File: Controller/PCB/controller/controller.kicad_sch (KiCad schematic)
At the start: 63 parts

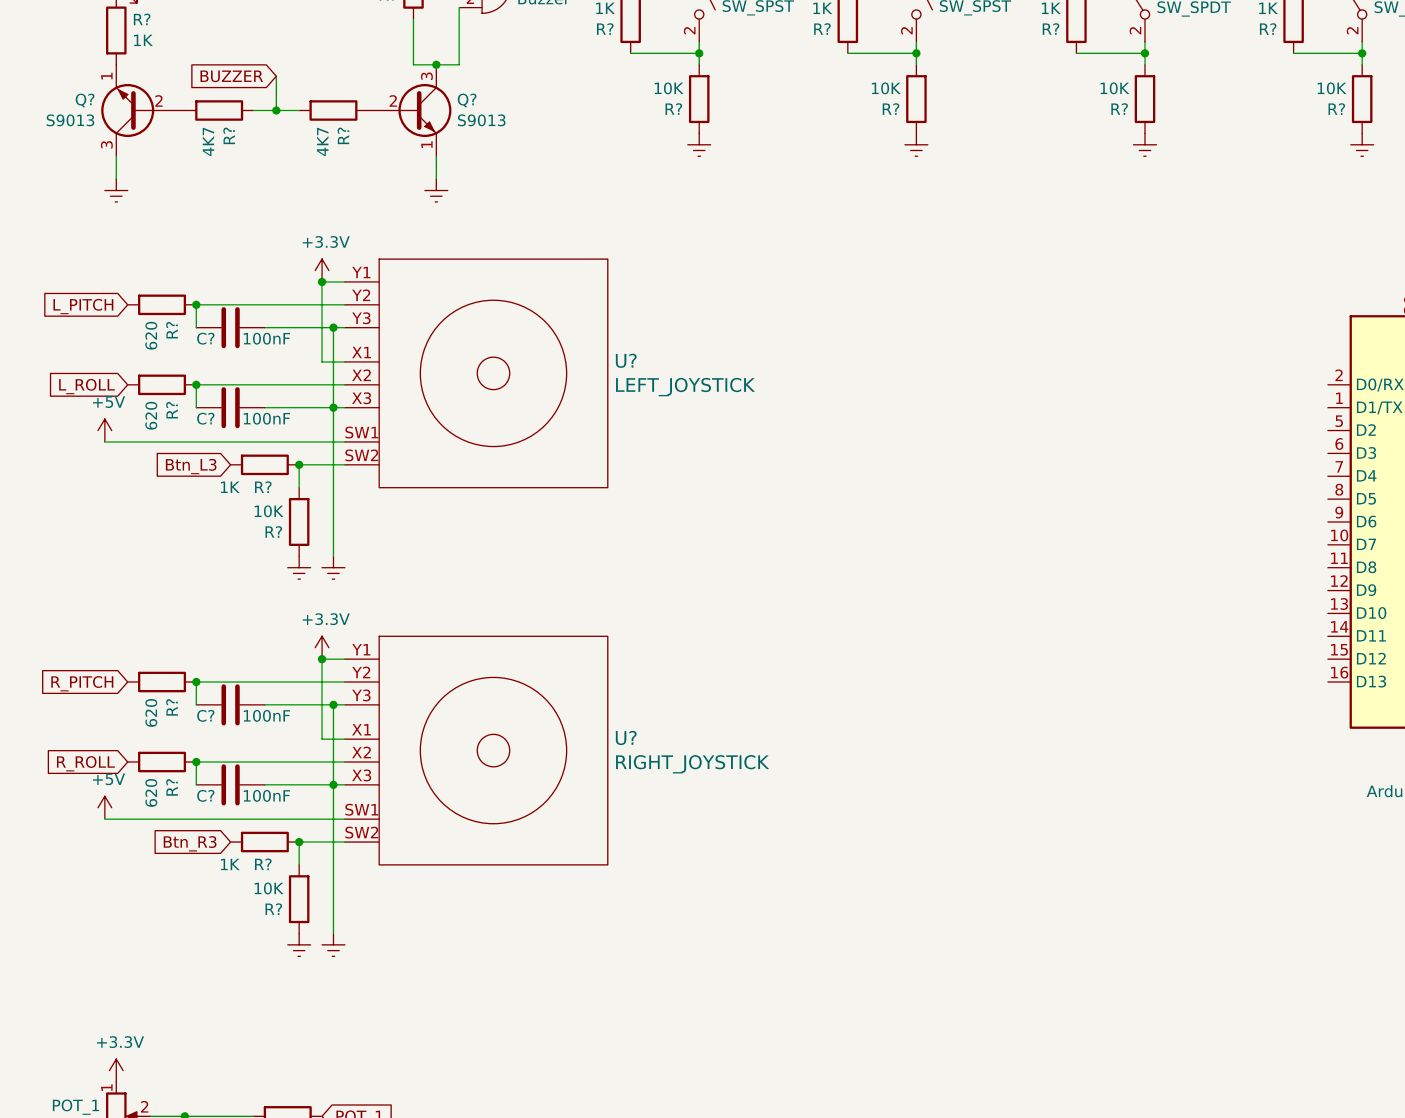
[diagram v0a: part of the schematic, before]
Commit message: Update git ignore and add make switches separate from the controller
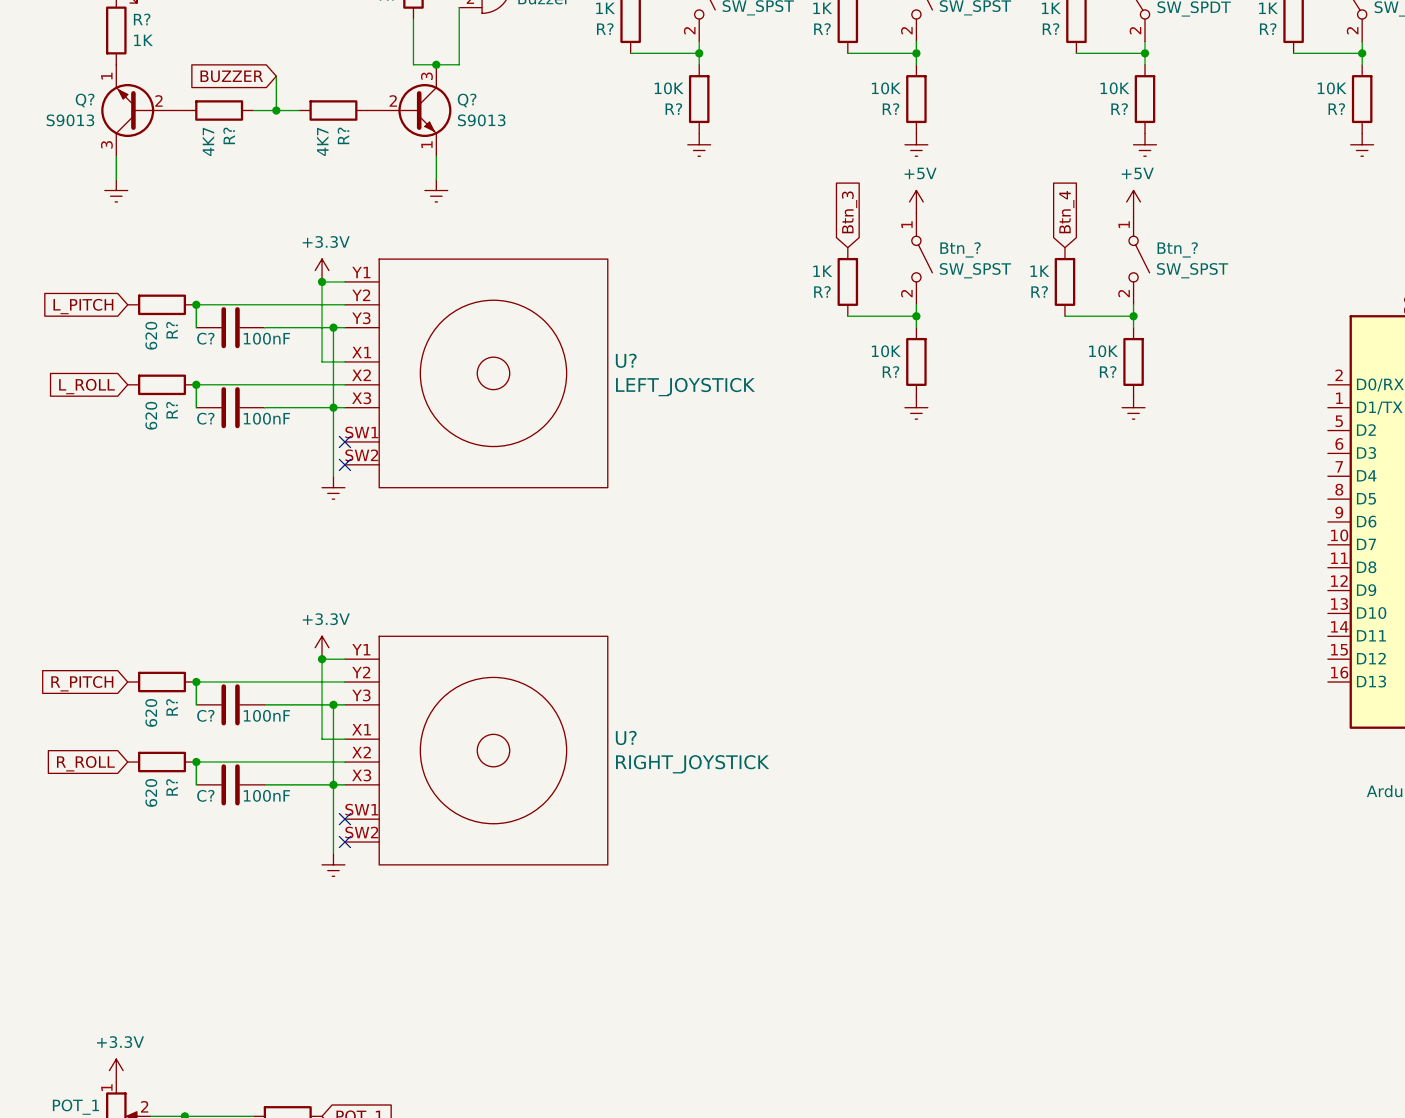
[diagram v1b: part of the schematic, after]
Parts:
- removed R? (x2): 1K, symbol Device:R
- removed R? (x2): 10K, symbol Device:R
- added Btn_? (x2): SW_SPST, symbol Switch:SW_SPST
- added R? (x2): 1K, symbol Device:R
- added R? (x2): 10K, symbol Device:R
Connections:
- net +5V: now also Btn_?.1 (A), Btn_?.1 (A); no longer U?.SW1, U?.SW1
- net Earth: now also R?.1, R?.1
- new net: Btn_?.2 (B), R?.1, R?.2 (x2)
- new net Btn_3: R?.2
- new net Btn_4: R?.2
- no-connect marks 3 -> 7

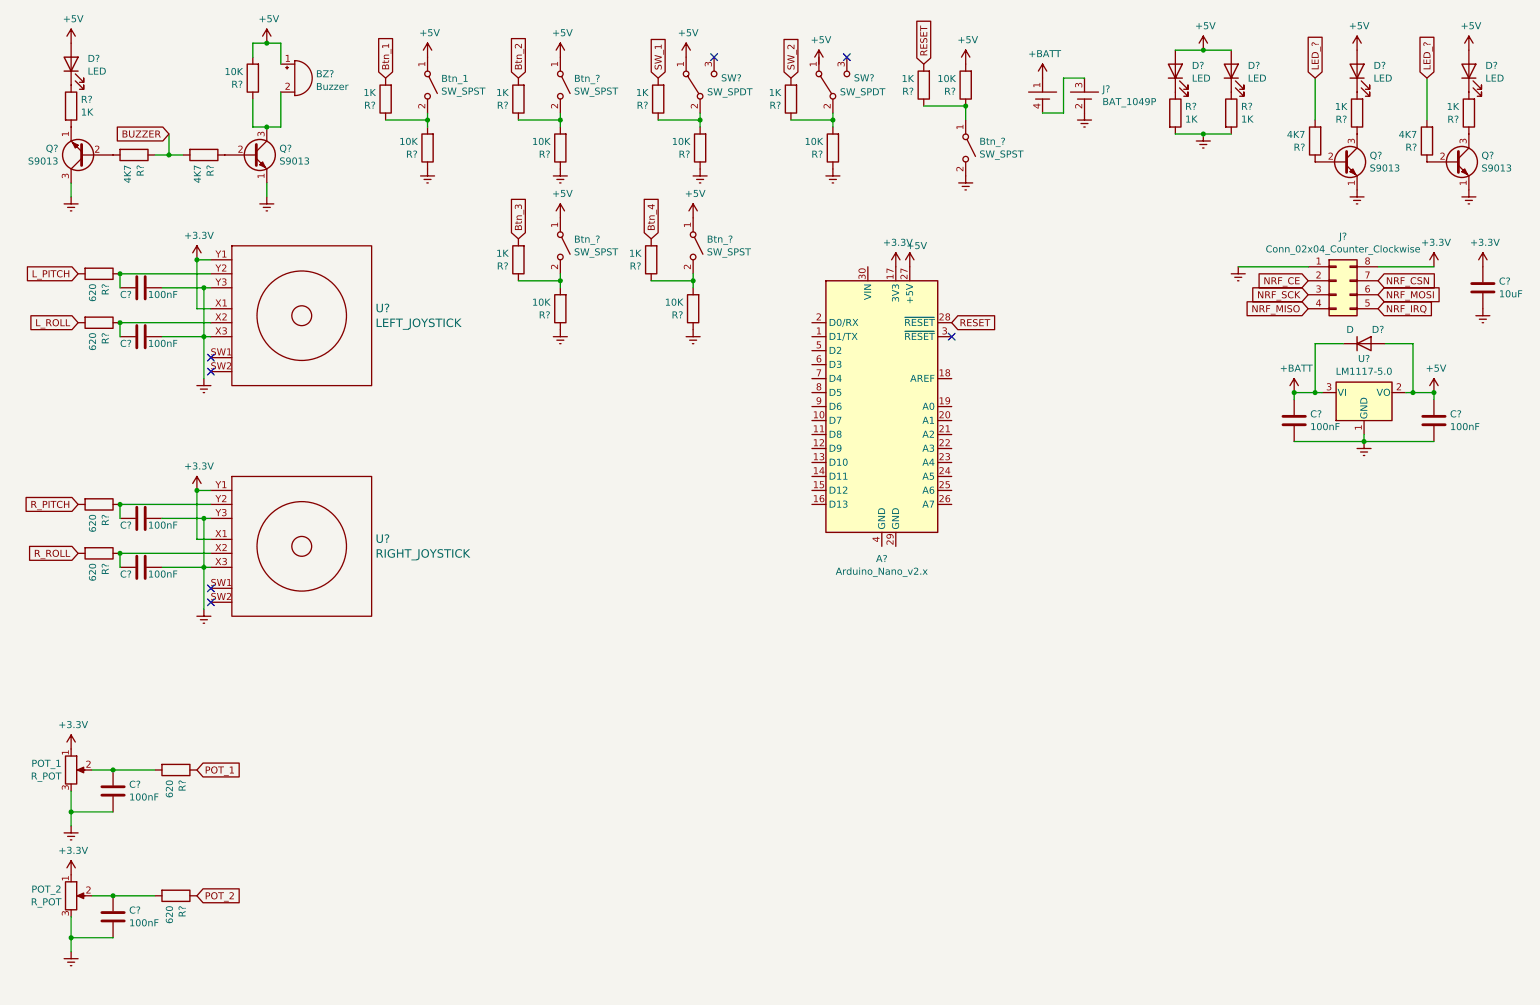
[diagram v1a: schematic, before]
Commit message: Update Component stuff
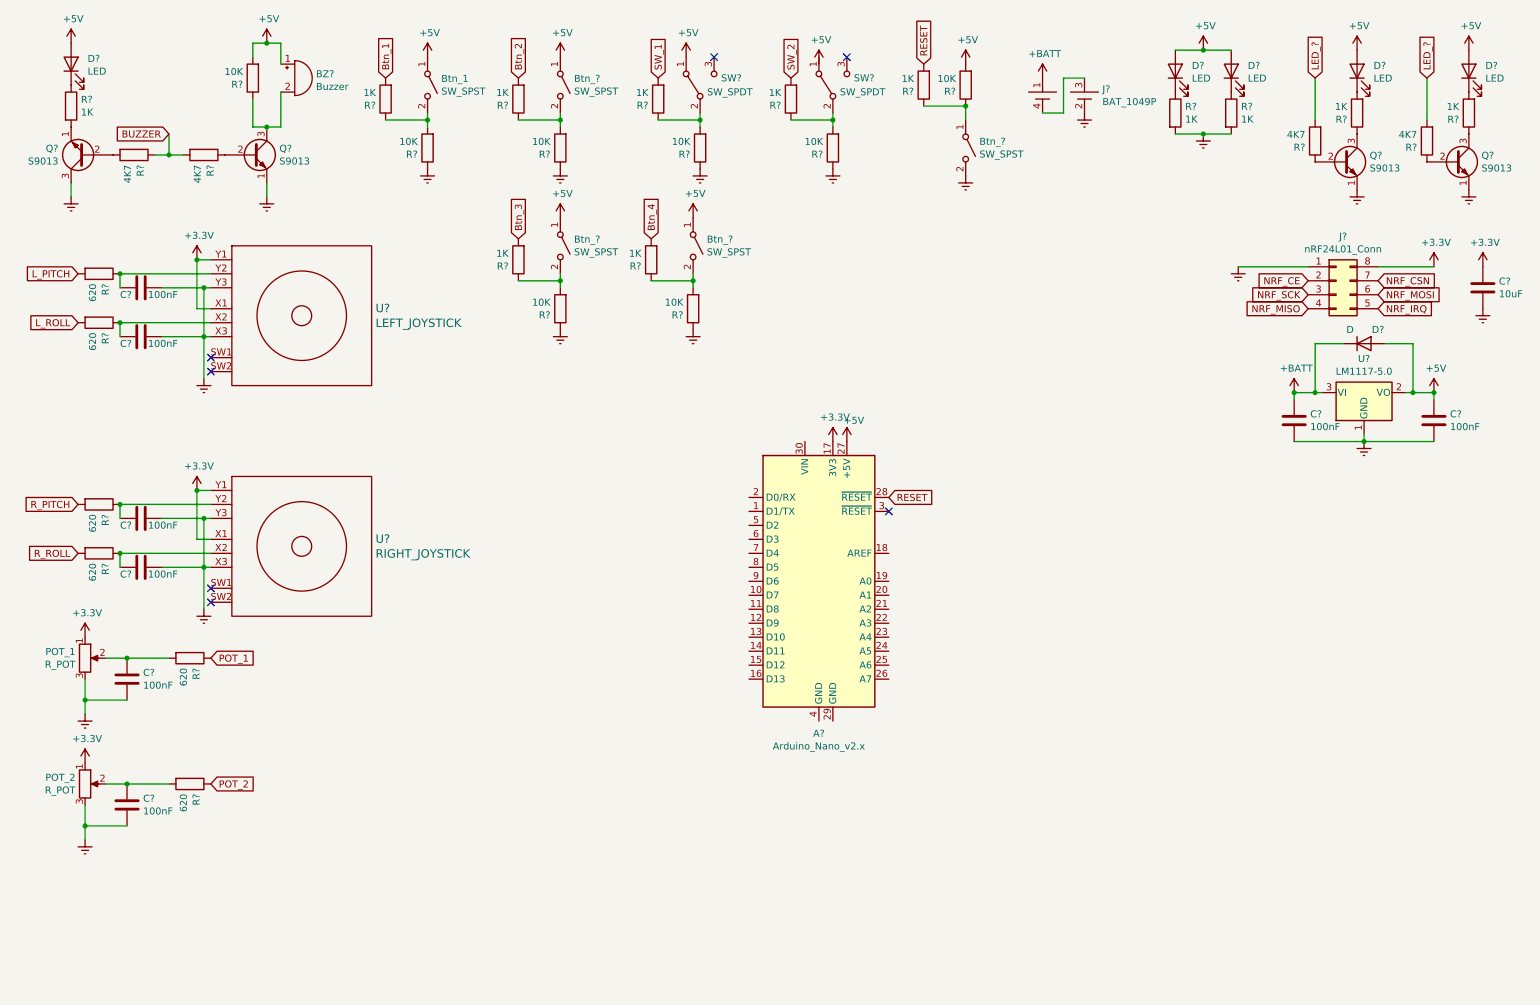
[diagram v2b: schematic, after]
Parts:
- J?: value Conn_02x04_Counter_Clockwise -> nRF24L01_Conn
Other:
- moved on the sheet: A?, C?, POT_1, POT_2, R?

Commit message: Update Schematic
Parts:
- removed D?: D, symbol Device:D
- removed J?: BAT_1049P, symbol TickerForge:BAT_1049P
- removed U?: LEFT_JOYSTICK, symbol TickerForge:JOYSTICK_BUTTON
- removed U?: RIGHT_JOYSTICK, symbol TickerForge:JOYSTICK_BUTTON
- added BT?: Bat_18650_x2, symbol My_Library.lib:Bat_18650_x2
- added D?: 1N5817, Diode_THT:D_DO-41_SOD81_P10.16mm_Horizontal, symbol Diode:1N5817
- added D?: BLUE_LED, symbol Device:LED
- added J?: SERIAL_DEBUG_CONNECTOR, symbol Connector_Generic:Conn_02x03_Counter_Clockwise
- added Q?: S9013, Package_TO_SOT_THT:TO-39-3, symbol Transistor_BJT:2N2219
- added R?: 1K, symbol Device:R
- added R? (x3): 10K, symbol Device:R
- added U?: NLAS4684, symbol My_Library.lib:NLAS4684
- added U?: Joystick, symbol My_Library.lib:Joystick
- added U?: Joystick, My_library:Joystick, symbol My_Library.lib:Joystick
- U?: value LM1117-5.0 -> LM2940-5.0
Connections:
- net +3V3: now also J?.6 (Pin_6), U?.X1, U?.X1, U?.Y1, U?.Y1
- net +5V: now also D?.2 (A)
- net +BATT: now also BT?., D?.1 (K)
- net Earth: now also Q?.1 (E), BT?., D?.2 (A), Q?.1 (E), U?.X3, U?.X3, U?.Y3, U?.Y3; no longer Q?.3 (C)
- net NRF_SCK: now also J?.2 (Pin_2)
- net at R?.2: now also Q?.3 (C); no longer Q?.1 (E)
- net at C?.2, R?.1: now also U?.X2 (x2)
- net at C?.2, R?.1: now also U?.Y2 (x2)
- new net: D?.1 (K), R?.1
- new net: Q?.3 (C), R?.2
- new net: Q?.2 (B), R?.1
- new net DEBUG: J?.1 (Pin_1), R?.1, R?.1, R?.2
- new net DEBUG_IRQ: J?.4 (Pin_4)
- new net DEBUG_MISO: J?.3 (Pin_3)
- new net DEBUG_MOSI: J?.5 (Pin_5)
- no-connect marks 7 -> 8
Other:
- moved on the sheet: A?, C?, Q?, U?

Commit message: Start PCB Schematic
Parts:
- removed BT?: Bat_18650_x2, symbol My_Library.lib:Bat_18650_x2
- removed C? (x6): 100nF, symbol Device:C
- removed D? (x4): LED, symbol Device:LED
- removed D?: BLUE_LED, symbol Device:LED
- removed Q? (x2): S9013, Package_TO_SOT_THT:TO-39-3, symbol Transistor_BJT:2N2219
- removed R? (x13): 1K, symbol Device:R
- removed R? (x4): 4K7, symbol Device:R
- removed R? (x9): 10K, symbol Device:R
- removed R? (x5): 620, symbol Device:R
- removed U?: NLAS4684, symbol My_Library.lib:NLAS4684
- removed U?: Joystick, symbol My_Library.lib:Joystick
- removed U?: Joystick, My_library:Joystick, symbol My_Library.lib:Joystick
- added BT1, BT2: Bat_18650, My_library:18650_Holder(1), symbol My_Library.lib:Bat_18650
- added C1, C2, C4, C5, C6, C8: 100nF, Capacitor_SMD:C_0603_1608Metric, symbol Device:C
- added D2, D3, D4, D5, D7, D8: LED, LED_SMD:LED_0603_1608Metric, symbol Device:LED
- added Q3, Q5: S9013, Package_TO_SOT_SMD:SOT-23, symbol Transistor_BJT:2N2219
- added R1, R11, R13, R14, R17, R19, R22, R24, R25, R27, R28, R29, R31, R33: 1K, Resistor_SMD:R_0603_1608Metric, symbol Device:R
- added R12, R15, R16, R20, R21, R23, R26: 10K, Resistor_SMD:R_0603_1608Metric, symbol Device:R
- added R3, R4, R5, R7, R8: 620, Resistor_SMD:R_0603_1608Metric, symbol Device:R
- added R30, R32, R6, R9: 4K7, Resistor_SMD:R_0603_1608Metric, symbol Device:R
- added U1, U2: Joystick, My_library:Joystick, symbol My_Library.lib:Joystick
- added U3, U4: NLAS4684, My_library:NLAS4684, symbol My_Library.lib:NLAS4684
- A1: renamed from A?; value Arduino_Nano_v2.x -> NUCLEO-L432KC
- BZ1: renamed from BZ?; footprint (none) -> Buzzer_Beeper:Buzzer_12x9.5RM7.6
- Btn_1: footprint (none) -> Button_Switch_SMD:SW_Push_1P1T_NO_6x6mm_H9.5mm
- Btn_2, Btn_3, Btn_4, Btn_5: renamed from Btn_?; footprint (none) -> Button_Switch_SMD:SW_Push_1P1T_NO_6x6mm_H9.5mm
- C3, C7: renamed from C?; footprint (none) -> Capacitor_SMD:C_0603_1608Metric
- D1: renamed from D?; footprint (none) -> LED_SMD:LED_0603_1608Metric
- D6: renamed from D?; footprint Diode_THT:D_DO-41_SOD81_P10.16mm_Horizontal -> My_library:1N5817M
- J1: renamed from J?; footprint (none) -> Connector_PinHeader_2.54mm:PinHeader_2x04_P2.54mm_Vertical_SMD
- J2: renamed from J?; footprint (none) -> Connector_PinHeader_2.54mm:PinHeader_2x03_P2.54mm_Vertical_SMD
- Q1, Q2, Q4: renamed from Q?; footprint Package_TO_SOT_THT:TO-39-3 -> Package_TO_SOT_SMD:SOT-23
- R10, R18, R2: renamed from R?; footprint (none) -> Resistor_SMD:R_0603_1608Metric
- U5: renamed from U?; footprint (none) -> Package_TO_SOT_SMD:SOT-223
- gave numbers to parts that had none: 3
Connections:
- net +3V3: now also U1.X1, U1.Y1, U2.X1, U2.Y1
- net +5V: now also C8.2, D4.2 (A), D5.2 (A), D7.2 (A), D8.2 (A), Q3.3 (C), R26.2, U3.1 (VCC), U4.1 (VCC), U4.3 (COM1)
- net +BATT: now also BT1.1
- net BUZZER: now also A1.20 (A1), R6.1, R9.2
- net Btn_1: now also A1.5 (D2), R11.2
- net Btn_2: now also A1.6 (D3), R13.2
- net Btn_3: now also A1.7 (D4), R14.2
- net Btn_4: now also A1.8 (D5), R17.2
- net DEBUG_IRQ: now also U4.10 (NO2)
- net DEBUG_MISO: now also U3.10 (NO2)
- net DEBUG_MOSI: now also U3.2 (NO1)
- net Earth: now also A1.29 (GND), A1.4 (GND), BT2.2, C1.2, C2.2, C4.1, C5.1, C6.1, C8.1, Q5.1 (E), R12.1, R15.1, R16.1, R20.1, R21.1, R23.1, R25.1, R27.1, R28.1, R29.1, U1.X3, U1.Y3, U2.X3, U2.Y3, U3.6 (GND), U4.6 (GND)
- net L_PITCH: now also A1.26 (A7)
- net L_ROLL: now also A1.25 (A6), R3.2
- net NRF_CE: now also A1.12 (D9)
- net NRF_CSN: now also A1.16 (D13)
- net NRF_IRQ: now also U4.7 (NC2)
- net NRF_MISO: now also U3.7 (NC2)
- net NRF_MOSI: now also U3.5 (NC1)
- net NRF_SCK: now also A1.13 (D10)
- net POT_1: now also A1.21 (A2), R7.1
- net POT_2: now also A1.22 (A3), R8.1
- net RESET: now also R24.2
- net R_PITCH: now also A1.24 (A5), R4.2
- net R_ROLL: now also A1.23 (A4), R5.2
- net SW_1: now also A1.9 (D6), R19.2
- net SW_2: now also A1.10 (D7), R22.2
- net at D1.1 (K): now also R1.2
- net at Q1.3 (C): now also R1.1
- net at Q1.2 (B): now also R6.2
- net at Q2.2 (B): now also R9.1
- net at Q4.3 (C): now also R31.1
- net at Q4.2 (B): now also R30.1
- net at Btn_5.1 (A): now also R24.1, R26.1
- net at POT_1.2: now also C1.1, R7.2
- net at POT_2.2: now also C2.1, R8.2
- net at SW1.2 (B): now also R19.1, R21.2
- net at SW2.2 (B): now also R22.1, R23.2
- net at C3.2, R2.1: now also U1.Y2
- net at Btn_1.2 (B): now also R11.1, R12.2
- net at Btn_2.2 (B): now also R13.1, R15.2
- net LED_2: now reaches A1.1 (D1/TX)
- net LED_2: now also R32.2
- net SERIAL_IRQ: now reaches A1.11 (D8)
- net SERIAL_IRQ: now also U4.9 (COM2)
- net SERIAL_MOSI: now reaches A1.14 (D11)
- net SERIAL_MOSI: now also U3.3 (COM1)
- net SERIAL_MISO: now reaches A1.15 (D12)
- net SERIAL_MISO: now also U3.9 (COM2)
- net LED_1: now reaches A1.2 (D0/RX)
- net LED_1: now also R30.2
- net at Btn_3.2 (B): now also R14.1, R16.2
- net at Btn_4.2 (B): now also R17.1, R20.2
- net at R18.2: now also Q3.2 (B)
- new net: C4.2, R3.1, U1.X2
- new net: D7.1 (K), R31.2
- new net: D2.2 (A), U4.2 (NO1)
- new net: Q3.1 (E), U3.4 (IN1), U3.8 (IN2), U4.4 (IN1), U4.8 (IN2)
- new net: D3.2 (A), U4.5 (NC1)
- new net: Q5.2 (B), R32.1
- new net: BT1.2, BT2.1
- new net: D3.1 (K), R27.2
- new net: D5.1 (K), R29.2
- new net: C6.2, R5.1, U2.X2
- new net: Q5.3 (C), R33.1
- new net: C5.2, R4.1, U2.Y2
- new net: D2.1 (K), R25.2
- new net: D4.1 (K), R28.2
- new net: D8.1 (K), R33.2
- no-connect marks 8 -> 9
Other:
- moved on the sheet: A1, R18

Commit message: Update Symbol Library
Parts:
- A1: footprint Module:Arduino_Nano -> My_library:NUCELO-L432KC_SMD
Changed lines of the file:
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@@
     (property "Reference" "A1" (id 0) (at 91.44 183.8706 0))
     (property "Value" "NUCLEO-L432KC" (id 1) (at 91.44 186.182 0))
-    (property "Footprint" "Module:Arduino_Nano" (id 2) (at 91.44 156.21 0)
+    (property "Footprint" "My_library:NUCELO-L432KC_SMD" (id 2) (at 91.44 156.21 0)
       (effects (font (size 1.27 1.27) italic) hide)
     )
@@
     )
     (path "/00000000-0000-0000-0000-000062120977"
-      (reference "A1") (unit 1) (value "NUCLEO-L432KC") (footprint "Module:Arduino_Nano")
+      (reference "A1") (unit 1) (value "NUCLEO-L432KC") (footprint "My_library:NUCELO-L432KC_SMD")
     )
     (path "/42f37560-b65a-4070-adca-823dfbc57e67"

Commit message: Minor Schematic Updates
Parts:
- removed J1: nRF24L01_Conn, Connector_PinHeader_2.54mm:PinHeader_2x04_P2.54mm_Vertical_SMD, symbol Connector_Generic:Conn_02x04_Counter_Clockwise
- removed J2: SERIAL_DEBUG_CONNECTOR, Connector_PinHeader_2.54mm:PinHeader_2x03_P2.54mm_Vertical_SMD, symbol Connector_Generic:Conn_02x03_Counter_Clockwise
- added J?: nRF24L01_Conn, symbol Connector_Generic:Conn_02x04_Odd_Even
- added J?: SERIAL_DEBUG_CONNECTOR, symbol Connector_Generic:Conn_02x06_Odd_Even
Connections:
- net +3V3: now also J?.2 (Pin_2), J?.6 (Pin_6), J?.7 (Pin_7)
- net DEBUG: now also J?.5 (Pin_5), J?.8 (Pin_8)
- net DEBUG_IRQ: now also J?.1 (Pin_1), J?.12 (Pin_12)
- net DEBUG_MISO: now also J?.11 (Pin_11), J?.2 (Pin_2)
- net DEBUG_MOSI: now also J?.10 (Pin_10), J?.3 (Pin_3)
- net Earth: now also J?.1 (Pin_1); no longer C9.2
- net NRF_CE: now also J?.3 (Pin_3)
- net NRF_CSN: now also J?.4 (Pin_4)
- net NRF_IRQ: now also J?.8 (Pin_8)
- net NRF_MISO: now also J?.7 (Pin_7)
- net NRF_MOSI: now also J?.6 (Pin_6)
- net NRF_SCK: now also J?.4 (Pin_4), J?.5 (Pin_5), J?.9 (Pin_9)
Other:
- moved on the sheet: C7, C8, D6, R18, U5
